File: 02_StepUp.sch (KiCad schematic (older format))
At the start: 25 parts, among them Q301 MMBT2222LT1G, Q302 TK7R7P10PL, U301 L7812, U302 UC3843_SOIC8

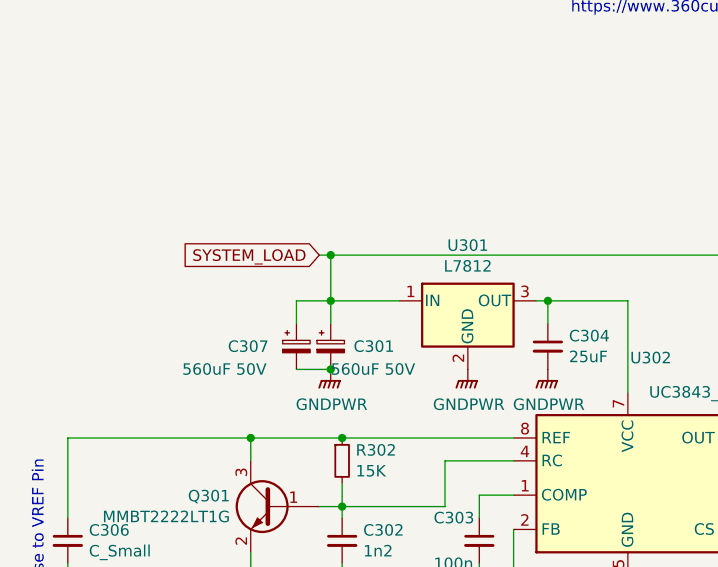
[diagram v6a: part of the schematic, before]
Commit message: Mountingholes und Heatsinks hinzugefügt
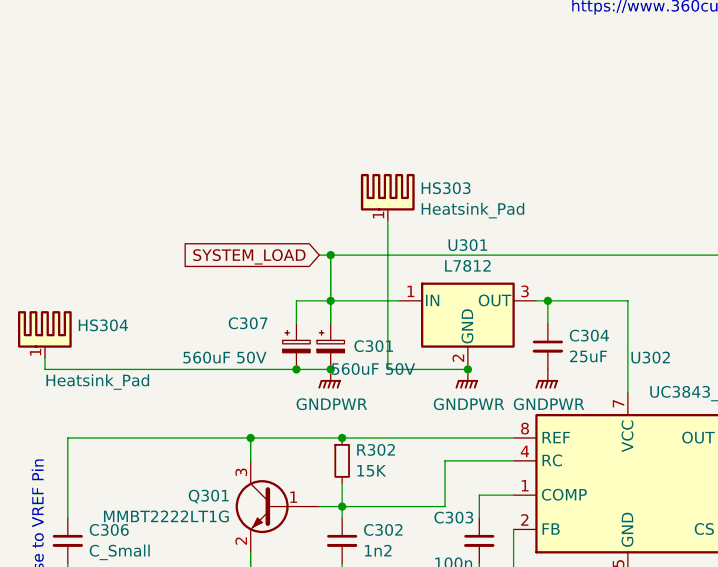
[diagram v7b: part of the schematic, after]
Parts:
- added HS303, HS304: Heatsink_Pad, Heatsink:Heatsink_AAVID_573300D00010G_TO-263, symbol Mechanical:Heatsink_Pad
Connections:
- net GNDPWR: now also HS303.1, HS304.1
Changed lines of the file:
@@
 AR Path="/5E751A81/5E9CD890" Ref="C?"  Part="1"
 AR Path="/5E73BAE8/5E9CD890" Ref="C307"  Part="1"
-F 0 "C307" H 3500 3000 50  0000 L CNN
-F 1 "560uF 50V" H 3300 2900 50  0000 L CNN
+F 0 "C307" H 3500 3100 50  0000 L CNN
+F 1 "560uF 50V" H 3300 2950 50  0000 L CNN
 F 2 "Capacitor_THT:CP_Radial_D12.5mm_P5.00mm" H 3800 3000 50  0001 C CNN
 F 3 "https://www.mouser.de/datasheet/2/420/United-Chemi-Con-1109128.pdf" H 3800 3000 50  0001 C CNN
@@
 	3800 3100 3950 3100
 Connection ~ 3950 3100
+$Comp
+L Mechanical:Heatsink_Pad HS303
+U 1 1 5E9A5BF9
+P 4200 2350
+F 0 "HS303" H 4341 2391 50  0000 L CNN
+F 1 "Heatsink_Pad" H 4341 2300 50  0000 L CNN
+F 2 "Heatsink:Heatsink_AAVID_573300D00010G_TO-263" H 4212 2300 50  0001 C CNN
+F 3 "~" H 4212 2300 50  0001 C CNN
+	1    4200 2350
+	1    0    0    -1
+$EndComp
+Wire Wire Line
+	4550 3100 4200 3100
+Wire Wire Line
+	4200 3100 4200 2450
+Connection ~ 4550 3100
+$Comp
+L Mechanical:Heatsink_Pad HS304
+U 1 1 5E9D1B13
+P 2700 2950
+F 0 "HS304" H 2841 2991 50  0000 L CNN
+F 1 "Heatsink_Pad" H 2700 2750 50  0000 L CNN
+F 2 "Heatsink:Heatsink_AAVID_573300D00010G_TO-263" H 2712 2900 50  0001 C CNN
+F 3 "~" H 2712 2900 50  0001 C CNN
+	1    2700 2950
+	1    0    0    -1
+$EndComp
+Wire Wire Line
+	2700 3050 2700 3100
+Wire Wire Line
+	2700 3100 3800 3100
+Connection ~ 3800 3100
 $EndSCHEMATC

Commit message: fertig zum routen
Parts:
- added J301, J302: Conn_02x04_Odd_Even, Connector_PinHeader_2.54mm:PinHeader_2x04_P2.54mm_Vertical, symbol Connector_Generic:Conn_02x04_Odd_Even
- HS301, HS302, HS303, HS304: value Heatsink_Pad -> 573300D00000G
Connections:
- net POWER_AMP: now also J302.2 (Pin_2), J302.4 (Pin_4), J302.6 (Pin_6), J302.8 (Pin_8); no longer C305.1, C308.1, D301.2 (K), HS301.1, RV301.1
- net SYSTEM_LOAD: now also J301.1 (Pin_1), J301.3 (Pin_3), J301.5 (Pin_5), J301.7 (Pin_7); no longer C301.1, C307.1, L301.1, R304.2, U301.1 (IN)
- new net: C301.1, C307.1, J301.2 (Pin_2), J301.4 (Pin_4), J301.6 (Pin_6), J301.8 (Pin_8), L301.1, R304.2, U301.1 (IN)
- new net: C305.1, C308.1, D301.2 (K), HS301.1, J302.1 (Pin_1), J302.3 (Pin_3), J302.5 (Pin_5), J302.7 (Pin_7), RV301.1
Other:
- note added: "F_osc = 1,72/(R_rc*C_rc)\nF_osc = 1,72/(15K*1n2)\nF_osc=95555Hz"
- note added: "Gate-Strom:\n95,5kHz*13nC =1,2mA"
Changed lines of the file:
@@
 	7900 3150 7600 3150
 Connection ~ 7400 3150
-Wire Wire Line
-	8250 3150 7900 3150
 Connection ~ 7900 3150
 $Comp
@@
 	6050 2600 6050 2800
 Connection ~ 6050 2600
-Text GLabel 3900 2600 0    50   Input ~ 0
+Text GLabel 3350 2600 0    50   Input ~ 0
 SYSTEM_LOAD
 $Comp
@@
 Connection ~ 3950 2600
 Wire Wire Line
-	3950 2600 6050 2600
+	3950 2600 5450 2600
 Wire Wire Line
 	4850 2800 4900 2800
@@
 Wire Wire Line
 	5900 4200 5900 3700
-Text GLabel 8250 3150 2    50   Output ~ 0
+Text GLabel 9150 3150 2    50   Output ~ 0
 POWER_AMP
 $Comp
@@
 P 7600 2700
 F 0 "HS301" H 7741 2741 50  0000 L CNN
-F 1 "Heatsink_Pad" H 7741 2650 50  0000 L CNN
+F 1 "573300D00000G" H 7741 2650 50  0000 L CNN
 F 2 "Heatsink:Heatsink_AAVID_573300D00010G_TO-263" H 7612 2650 50  0001 C CNN
-F 3 "~" H 7612 2650 50  0001 C CNN
+F 3 "https://www.mouser.de/datasheet/2/2/Aavid-Board-Level-Heatsinks-Catalog-2018-1507171.pdf" H 7612 2650 50  0001 C CNN
 	1    7600 2700
 	1    0    0    -1
@@
 P 6400 2450
 F 0 "HS302" H 6541 2491 50  0000 L CNN
-F 1 "Heatsink_Pad" H 6541 2400 50  0000 L CNN
+F 1 "573300D00000G" H 6541 2400 50  0000 L CNN
 F 2 "Heatsink:Heatsink_AAVID_573300D00010G_TO-263" H 6412 2400 50  0001 C CNN
-F 3 "~" H 6412 2400 50  0001 C CNN
+F 3 "https://www.mouser.de/datasheet/2/2/Aavid-Board-Level-Heatsinks-Catalog-2018-1507171.pdf" H 6412 2400 50  0001 C CNN
 	1    6400 2450
 	1    0    0    -1
@@
 P 4200 2350
 F 0 "HS303" H 4341 2391 50  0000 L CNN
-F 1 "Heatsink_Pad" H 4341 2300 50  0000 L CNN
+F 1 "573300D00000G" H 4341 2300 50  0000 L CNN
 F 2 "Heatsink:Heatsink_AAVID_573300D00010G_TO-263" H 4212 2300 50  0001 C CNN
-F 3 "~" H 4212 2300 50  0001 C CNN
+F 3 "https://www.mouser.de/datasheet/2/2/Aavid-Board-Level-Heatsinks-Catalog-2018-1507171.pdf" H 4212 2300 50  0001 C CNN
 	1    4200 2350
 	1    0    0    -1
@@
 P 2700 2950
 F 0 "HS304" H 2841 2991 50  0000 L CNN
-F 1 "Heatsink_Pad" H 2700 2750 50  0000 L CNN
+F 1 "573300D00000G" H 2700 2750 50  0000 L CNN
 F 2 "Heatsink:Heatsink_AAVID_573300D00010G_TO-263" H 2712 2900 50  0001 C CNN
-F 3 "~" H 2712 2900 50  0001 C CNN
+F 3 "https://www.mouser.de/datasheet/2/2/Aavid-Board-Level-Heatsinks-Catalog-2018-1507171.pdf" H 2712 2900 50  0001 C CNN
 	1    2700 2950
 	1    0    0    -1
@@
 	2700 3100 3800 3100
 Connection ~ 3800 3100
+Wire Wire Line
+	3400 2600 3350 2600
+Wire Wire Line
+	7900 3150 8450 3150
+Wire Wire Line
+	9150 3150 8950 3150
+Text Notes 3750 4850 0    50   ~ 0
+F_osc = 1,72/(R_rc*C_rc)\nF_osc = 1,72/(15K*1n2)\nF_osc=95555Hz
+Text Notes 5800 4850 0    50   ~ 0
+Gate-Strom:\n95,5kHz*13nC =1,2mA
+$Comp
+L Connector_Generic:Conn_02x04_Odd_Even J301
+U 1 1 5EA860C7
+P 3600 2400
+F 0 "J301" H 3650 2717 50  0000 C CNN
+F 1 "Conn_02x04_Odd_Even" H 3650 2626 50  0000 C CNN
+F 2 "Connector_PinHeader_2.54mm:PinHeader_2x04_P2.54mm_Vertical" H 3600 2400 50  0001 C CNN
+F 3 "~" H 3600 2400 50  0001 C CNN
+	1    3600 2400
+	1    0    0    -1
+$EndComp
+Wire Wire Line
+	3400 2500 3400 2600
+Wire Wire Line
+	3900 2500 3900 2600
+Connection ~ 3400 2600
+Connection ~ 3900 2600
+$Comp
+L Connector_Generic:Conn_02x04_Odd_Even J302
+U 1 1 5EA865EB
+P 8650 2950
+F 0 "J302" H 8700 3267 50  0000 C CNN
+F 1 "Conn_02x04_Odd_Even" H 8700 3176 50  0000 C CNN
+F 2 "Connector_PinHeader_2.54mm:PinHeader_2x04_P2.54mm_Vertical" H 8650 2950 50  0001 C CNN
+F 3 "~" H 8650 2950 50  0001 C CNN
+	1    8650 2950
+	1    0    0    -1
+$EndComp
+Wire Wire Line
+	8450 3050 8450 3150
+Wire Wire Line
+	8950 3050 8950 3150
+Connection ~ 8450 3150
+Connection ~ 8950 3150
+Wire Wire Line
+	8950 2850 8950 2950
+Connection ~ 8950 3050
+Connection ~ 8950 2950
+Wire Wire Line
+	8950 2950 8950 3050
+Wire Wire Line
+	8450 2850 8450 2950
+Connection ~ 8450 3050
+Connection ~ 8450 2950
+Wire Wire Line
+	8450 2950 8450 3050
+Wire Wire Line
+	3900 2300 3900 2400
+Connection ~ 3900 2500
+Connection ~ 3900 2400
+Wire Wire Line
+	3900 2400 3900 2500
+Wire Wire Line
+	3400 2300 3400 2400
+Connection ~ 3400 2500
+Connection ~ 3400 2400
+Wire Wire Line
+	3400 2400 3400 2500
+$Comp
+L power:PWR_FLAG #FLG0113
+U 1 1 5E9902DB
+P 5450 2600
+F 0 "#FLG0113" H 5450 2675 50  0001 C CNN
+F 1 "PWR_FLAG" H 5450 2774 50  0000 C CNN
+F 2 "" H 5450 2600 50  0001 C CNN
+F 3 "~" H 5450 2600 50  0001 C CNN
+	1    5450 2600
+	1    0    0    -1
+$EndComp
+Connection ~ 5450 2600
+Wire Wire Line
+	5450 2600 6050 2600
 $EndSCHEMATC
